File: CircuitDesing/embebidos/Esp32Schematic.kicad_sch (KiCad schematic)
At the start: 5 parts, among them U1 ESP32-WROOM-32

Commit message: Avance esquemático
Subcircuitos
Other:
- note added: "*NR ND"
- note added: "Pendiente de consulta"
- moved on the sheet: C1, C2, C3, R1, U1

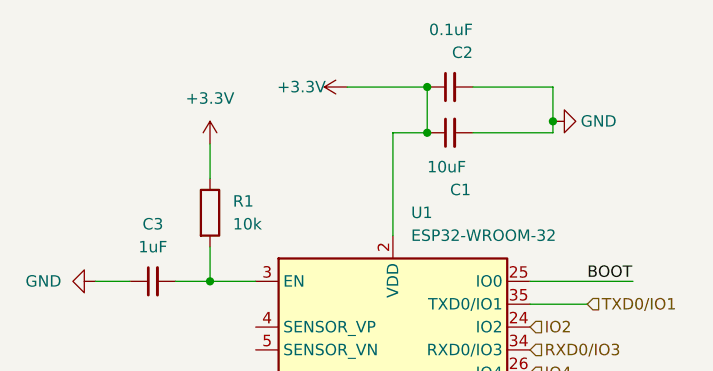
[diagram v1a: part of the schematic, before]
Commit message: Potencia
Primera propuesta del esquema de potencia
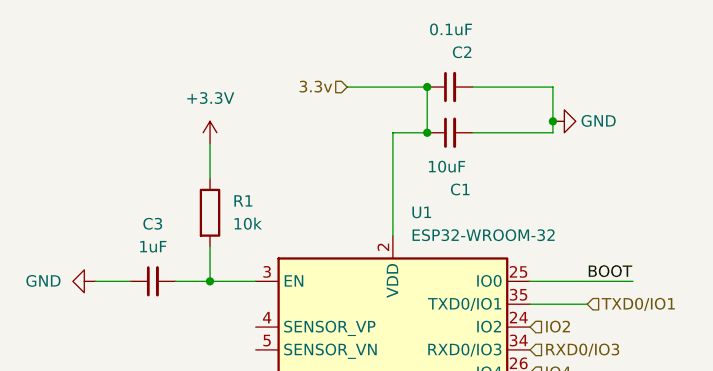
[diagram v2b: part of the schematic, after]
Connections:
- net +3.3V: no longer C1.1, C2.1, U1.2 (VDD)
- new net 3.3v: C1.1, C2.1, U1.2 (VDD)
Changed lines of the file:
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@@
     (effects (font (size 1.27 1.27)) (justify left))
+  )
+  (hierarchical_label "3.3v" (shape input) (at 78.74 48.26 180)
+    (effects (font (size 1.27 1.27)) (justify right))
   )
   (hierarchical_label "IO35" (shape input) (at 99.06 128.27 0)
@@
       (effects (font (size 1.27 1.27)) hide)
     )
-    (pin "1")
-  )
-  (symbol (lib_id "power:+3.3V") (at 78.74 48.26 90) (unit 1)
-    (in_bom yes) (on_board yes)
-    (property "Reference" "#PWR0101" (id 0) (at 82.55 48.26 0)
-      (effects (font (size 1.27 1.27)) hide)
-    )
-    (property "Value" "+3.3V" (id 1) (at 73.66 48.26 90))
-    (property "Footprint" "" (id 2) (at 78.74 48.26 0)
-      (effects (font (size 1.27 1.27)) hide)
-    )
-    (property "Datasheet" "" (id 3) (at 78.74 48.26 0)
-      (effects (font (size 1.27 1.27)) hide)
-    )

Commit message: Bootoption enable sw
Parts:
- added SW1, SW2: SW_Push, symbol Switch:SW_Push
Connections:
- net BOOT: now also SW2.1
- net GND: now also SW1.1, SW2.2
- net at C3.2, R1.2, U1.3 (EN): now also SW1.2
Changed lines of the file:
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@@
   (junction (at 63.5 69.85) (diameter 0) (color 0 0 0 0)
   )
+  (junction (at 52.07 69.85) (diameter 0) (color 0 0 0 0)
+  )
   (junction (at 101.6 52.07) (diameter 0) (color 0 0 0 0)
   )
@@
     (stroke (width 0) (type default) (color 0 0 0 0))
   )
+  (wire (pts (xy 63.5 69.85) (xy 63.5 78.74))
+    (stroke (width 0) (type default) (color 0 0 0 0))
+  )
   (wire (pts (xy 105.41 72.39) (xy 99.06 72.39))
     (stroke (width 0) (type default) (color 0 0 0 0))
   )
+  (wire (pts (xy 52.07 69.85) (xy 52.07 80.01))
+    (stroke (width 0) (type default) (color 0 0 0 0))
+  )
+  (wire (pts (xy 63.5 78.74) (xy 62.23 80.01))
+    (stroke (width 0) (type default) (color 0 0 0 0))
+  )
   (wire (pts (xy 59.69 69.85) (xy 63.5 69.85))
     (stroke (width 0) (type default) (color 0 0 0 0))
@@
     (stroke (width 0) (type default) (color 0 0 0 0))
   )
+  (wire (pts (xy 52.07 69.85) (xy 54.61 69.85))
+    (stroke (width 0) (type default) (color 0 0 0 0))
+  )
+  (wire (pts (xy 116.84 68.58) (xy 110.49 68.58))
+    (stroke (width 0) (type default) (color 0 0 0 0))
+  )
   (wire (pts (xy 63.5 54.61) (xy 63.5 58.42))
     (stroke (width 0) (type default) (color 0 0 0 0))
   )
-  (wire (pts (xy 50.8 69.85) (xy 54.61 69.85))
+  (wire (pts (xy 50.8 69.85) (xy 52.07 69.85))
+    (stroke (width 0) (type default) (color 0 0 0 0))
+  )
+  (wire (pts (xy 110.49 68.58) (xy 110.49 69.85))
     (stroke (width 0) (type default) (color 0 0 0 0))
   )
@@
   (hierarchical_label "IO16" (shape input) (at 99.06 95.25 0)
     (effects (font (size 1.27 1.27)) (justify left))
+  )
+  (symbol (lib_id "power:GND") (at 50.8 69.85 270) (unit 1)
+    (in_bom yes) (on_board yes) (fields_autoplaced)
+    (property "Reference" "#PWR?" (id 0) (at 44.45 69.85 0)
+      (effects (font (size 1.27 1.27)) hide)
+    )
+    (property "Value" "GND" (id 1) (at 46.99 69.8499 90)
+      (effects (font (size 1.27 1.27)) (justify right))
+    )
+    (property "Footprint" "" (id 2) (at 50.8 69.85 0)
+      (effects (font (size 1.27 1.27)) hide)
+    )
+    (property "Datasheet" "" (id 3) (at 50.8 69.85 0)
+      (effects (font (size 1.27 1.27)) hide)
+    )
+    (pin "1")
   )
   (symbol (lib_id "power:GND") (at 83.82 137.16 0) (unit 1)
@@
     (pin "1")
   )
+  (symbol (lib_id "Switch:SW_Push") (at 121.92 68.58 0) (unit 1)
+    (in_bom yes) (on_board yes) (fields_autoplaced)
+    (property "Reference" "SW2" (id 0) (at 121.92 60.96 0))
+    (property "Value" "SW_Push" (id 1) (at 121.92 63.5 0))
+    (property "Footprint" "" (id 2) (at 121.92 63.5 0)
+      (effects (font (size 1.27 1.27)) hide)
+    )
+    (property "Datasheet" "~" (id 3) (at 121.92 63.5 0)
+      (effects (font (size 1.27 1.27)) hide)
+    )
+    (pin "1")
+    (pin "2")
+  )
+  (symbol (lib_id "power:GND") (at 127 68.58 90) (unit 1)
+    (in_bom yes) (on_board yes) (fields_autoplaced)
+    (property "Reference" "#PWR?" (id 0) (at 133.35 68.58 0)
+      (effects (font (size 1.27 1.27)) hide)
+    )
+    (property "Value" "GND" (id 1) (at 130.81 68.5799 90)
+      (effects (font (size 1.27 1.27)) (justify right))
+    )
+    (property "Footprint" "" (id 2) (at 127 68.58 0)
+      (effects (font (size 1.27 1.27)) hide)
+    )
+    (property "Datasheet" "" (id 3) (at 127 68.58 0)
+      (effects (font (size 1.27 1.27)) hide)
+    )
+    (pin "1")
+  )
   (symbol (lib_id "Device:R") (at 63.5 62.23 0) (unit 1)
     (in_bom yes) (on_board yes) (fields_autoplaced)
@@
     (pin "1")
   )
-  (symbol (lib_id "power:GND") (at 50.8 69.85 270) (unit 1)
-    (in_bom yes) (on_board yes) (fields_autoplaced)
-    (property "Reference" "#PWR0104" (id 0) (at 44.45 69.85 0)
-      (effects (font (size 1.27 1.27)) hide)
-    )
-    (property "Value" "GND" (id 1) (at 46.99 69.8499 90)
-      (effects (font (size 1.27 1.27)) (justify right))
-    )
-    (property "Footprint" "" (id 2) (at 50.8 69.85 0)
-      (effects (font (size 1.27 1.27)) hide)
-    )
-    (property "Datasheet" "" (id 3) (at 50.8 69.85 0)
-      (effects (font (size 1.27 1.27)) hide)
-    )
-    (pin "1")
+  (symbol (lib_id "Switch:SW_Push") (at 57.15 80.01 0) (unit 1)
+    (in_bom yes) (on_board yes) (fields_autoplaced)
+    (property "Reference" "SW1" (id 0) (at 57.15 72.39 0))
+    (property "Value" "SW_Push" (id 1) (at 57.15 74.93 0))
+    (property "Footprint" "" (id 2) (at 57.15 74.93 0)
+      (effects (font (size 1.27 1.27)) hide)
+    )
+    (property "Datasheet" "~" (id 3) (at 57.15 74.93 0)
+      (effects (font (size 1.27 1.27)) hide)
+    )
+    (pin "1")
+    (pin "2")
   )
   (symbol (lib_id "Device:C_Small") (at 57.15 69.85 90) (unit 1)

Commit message: Huellas parciales
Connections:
- net +3.3V is gone; now on net 3.3v: R1.1
- no-connect marks 0 -> 8
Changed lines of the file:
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@@
   (junction (at 101.6 52.07) (diameter 0) (color 0 0 0 0)
   )
+  (no_connect (at 68.58 107.95))
+  (no_connect (at 68.58 110.49))
+  (no_connect (at 68.58 113.03))
+  (no_connect (at 68.58 77.47))
+  (no_connect (at 68.58 74.93))
+  (no_connect (at 68.58 100.33))
+  (no_connect (at 68.58 102.87))
+  (no_connect (at 68.58 105.41))
   (wire (pts (xy 92.71 53.34) (xy 101.6 53.34))
     (stroke (width 0) (type default) (color 0 0 0 0))
@@
     (effects (font (size 1.27 1.27)) (justify left))
   )
+  (hierarchical_label "3.3v" (shape input) (at 63.5 54.61 180)
+    (effects (font (size 1.27 1.27)) (justify right))
+  )
   (hierarchical_label "IO4" (shape input) (at 99.06 80.01 0)
     (effects (font (size 1.27 1.27)) (justify left))
@@
   (symbol (lib_id "power:GND") (at 50.8 69.85 270) (unit 1)
     (in_bom yes) (on_board yes) (fields_autoplaced)
-    (property "Reference" "#PWR?" (id 0) (at 44.45 69.85 0)
+    (property "Reference" "#PWR01" (id 0) (at 44.45 69.85 0)
       (effects (font (size 1.27 1.27)) hide)
     )
@@
     (pin "9")
   )
-  (symbol (lib_id "power:+3.3V") (at 63.5 54.61 0) (unit 1)
-    (in_bom yes) (on_board yes) (fields_autoplaced)
-    (property "Reference" "#PWR0102" (id 0) (at 63.5 58.42 0)
-      (effects (font (size 1.27 1.27)) hide)
-    )
-    (property "Value" "+3.3V" (id 1) (at 63.5 49.53 0))
-    (property "Footprint" "" (id 2) (at 63.5 54.61 0)
-      (effects (font (size 1.27 1.27)) hide)
-    )
-    (property "Datasheet" "" (id 3) (at 63.5 54.61 0)
-      (effects (font (size 1.27 1.27)) hide)
-    )
-    (pin "1")
-  )
   (symbol (lib_id "Switch:SW_Push") (at 121.92 68.58 0) (unit 1)
     (in_bom yes) (on_board yes) (fields_autoplaced)
@@
   (symbol (lib_id "power:GND") (at 127 68.58 90) (unit 1)
     (in_bom yes) (on_board yes) (fields_autoplaced)
-    (property "Reference" "#PWR?" (id 0) (at 133.35 68.58 0)
-      (effects (font (size 1.27 1.27)) hide)
-    )
+    (property "Reference" "#PWR02" (id 0) (at 133.35 68.58 0)
+      (effects (font (size 1.27 1.27)) hide)
+    )

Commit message: Todas las huellas
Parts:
- SW1, SW2: footprint (none) -> Button_Switch_SMD:SW_SPST_EVQP0
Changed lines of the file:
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@@
     (property "Reference" "SW2" (id 0) (at 121.92 60.96 0))
     (property "Value" "SW_Push" (id 1) (at 121.92 63.5 0))
-    (property "Footprint" "" (id 2) (at 121.92 63.5 0)
+    (property "Footprint" "Button_Switch_SMD:SW_SPST_EVQP0" (id 2) (at 121.92 63.5 0)
       (effects (font (size 1.27 1.27)) hide)
     )
@@
     (property "Reference" "SW1" (id 0) (at 57.15 72.39 0))
     (property "Value" "SW_Push" (id 1) (at 57.15 74.93 0))
-    (property "Footprint" "" (id 2) (at 57.15 74.93 0)
+    (property "Footprint" "Button_Switch_SMD:SW_SPST_EVQP0" (id 2) (at 57.15 74.93 0)
       (effects (font (size 1.27 1.27)) hide)
     )

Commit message: Actualizacion huellas
Huellas+Programador
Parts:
- added C4: 1uF, Capacitor_SMD:C_0603_1608Metric_Pad1.08x0.95mm_HandSolder, symbol Device:C_Small
- added R8: 10k, Resistor_SMD:R_0603_1608Metric_Pad0.98x0.95mm_HandSolder, symbol Device:R
- C1: value 10uF -> 1uF
- C3: value 1uF -> 10uF
- SW1, SW2: footprint Button_Switch_SMD:SW_SPST_EVQP0 -> Button_Switch_SMD:SW_Push_1P1T_NO_6x6mm_H9.5mm
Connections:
- net 3.3v: now also C3.1, R8.1; no longer C1.1
- net BOOT: now also C4.1, R8.2
- net GND: now also C1.1, C3.2, C4.2; no longer C1.2, C3.1
- net at R1.2, SW1.2, U1.3 (EN): now also C1.2; no longer C3.2
- net LedU: now reaches U1.5 (SENSOR_VN)
- no-connect marks 8 -> 7
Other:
- note added: "Boot-Programar"
- note added: "Enable-Programar"
- note removed: "*NR ND"
- note removed: "Pendiente de consulta"

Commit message: Ruteo completo
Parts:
- renumbered SW2 to BOOT1, SW1 to EN1, R8 to R2
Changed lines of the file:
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@@
   (symbol (lib_id "Switch:SW_Push") (at 129.54 64.77 0) (unit 1)
     (in_bom yes) (on_board yes) (fields_autoplaced)
-    (property "Reference" "SW2" (id 0) (at 129.54 57.15 0))
+    (property "Reference" "BOOT1" (id 0) (at 129.54 57.15 0))
     (property "Value" "SW_Push" (id 1) (at 129.54 59.69 0))
     (property "Footprint" "Button_Switch_SMD:SW_Push_1P1T_NO_6x6mm_H9.5mm" (id 2) (at 129.54 59.69 0)
@@
   (symbol (lib_id "Device:R") (at 109.22 57.15 0) (unit 1)
     (in_bom yes) (on_board yes) (fields_autoplaced)
-    (property "Reference" "R8" (id 0) (at 111.76 55.8799 0)
+    (property "Reference" "R2" (id 0) (at 111.76 55.8799 0)
       (effects (font (size 1.27 1.27)) (justify left))
     )
@@
   (symbol (lib_id "power:GND") (at 87.63 132.08 0) (unit 1)
     (in_bom yes) (on_board yes) (fields_autoplaced)
-    (property "Reference" "#PWR0106" (id 0) (at 87.63 138.43 0)
+    (property "Reference" "#PWR09" (id 0) (at 87.63 138.43 0)
       (effects (font (size 1.27 1.27)) hide)
     )
@@
   (symbol (lib_id "power:GND") (at 138.43 64.77 90) (unit 1)
     (in_bom yes) (on_board yes) (fields_autoplaced)
-    (property "Reference" "#PWR0107" (id 0) (at 144.78 64.77 0)
+    (property "Reference" "#PWR011" (id 0) (at 144.78 64.77 0)
       (effects (font (size 1.27 1.27)) hide)
     )
@@
   (symbol (lib_id "power:GND") (at 45.72 64.77 270) (unit 1)
     (in_bom yes) (on_board yes) (fields_autoplaced)
-    (property "Reference" "#PWR0104" (id 0) (at 39.37 64.77 0)
+    (property "Reference" "#PWR08" (id 0) (at 39.37 64.77 0)
       (effects (font (size 1.27 1.27)) hide)
     )
@@
   (symbol (lib_id "power:GND") (at 111.76 45.72 90) (unit 1)
     (in_bom yes) (on_board yes)
-    (property "Reference" "#PWR0105" (id 0) (at 118.11 45.72 0)
+    (property "Reference" "#PWR010" (id 0) (at 118.11 45.72 0)
       (effects (font (size 1.27 1.27)) hide)
     )
@@
   (symbol (lib_id "Switch:SW_Push") (at 55.88 74.93 0) (unit 1)
     (in_bom yes) (on_board yes) (fields_autoplaced)
-    (property "Reference" "SW1" (id 0) (at 55.88 67.31 0))
+    (property "Reference" "EN1" (id 0) (at 55.88 67.31 0))
     (property "Value" "SW_Push" (id 1) (at 55.88 69.85 0))
     (property "Footprint" "Button_Switch_SMD:SW_Push_1P1T_NO_6x6mm_H9.5mm" (id 2) (at 55.88 69.85 0)
